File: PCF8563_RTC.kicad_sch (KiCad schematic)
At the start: 28 parts, among them J1 CONN_2P, J2 CONN_2P, J3 CONN_2P, J4 CONN_2P, J5 CONN_2P, J6 CONN_2P, J7 CONN_2P, U1 PCF8563, X1 32.768 kHz

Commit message: Created footprints for the PCF8563-SO8 package and capacitors
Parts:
- C1, C2, C3, C4: footprint (none) -> workshop_footprints:C0603
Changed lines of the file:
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@@
       (effects (font (size 1.27 1.27)) (justify right))
     )
-    (property "Footprint" "" (id 2) (at 61.595 50.8 0)
+    (property "Footprint" "workshop_footprints:C0603" (id 2) (at 61.595 50.8 0)
       (effects (font (size 1.27 1.27)) hide)
     )
@@
       (effects (font (size 1.27 1.27)) (justify right))
     )
-    (property "Footprint" "" (id 2) (at 32.385 116.84 0)
+    (property "Footprint" "workshop_footprints:C0603" (id 2) (at 32.385 116.84 0)
       (effects (font (size 1.27 1.27)) hide)
     )
@@
     (pin "2")
   )
-  (symbol (lib_id "WorkshopSymbols:C") (at 98.425 88.9 90) (unit 1)
+  (symbol (lib_name "C_3") (lib_id "WorkshopSymbols:C") (at 98.425 88.9 90) (unit 1)
     (in_bom yes) (on_board yes)
     (property "Reference" "C4" (id 0) (at 100.965 87.6299 90)
@@
       (effects (font (size 1.27 1.27)) (justify right))
     )
-    (property "Footprint" "" (id 2) (at 94.615 93.98 0)
+    (property "Footprint" "workshop_footprints:C0603" (id 2) (at 94.615 93.98 0)
       (effects (font (size 1.27 1.27)) hide)
     )
@@
       (effects (font (size 1.27 1.27)) (justify right))
     )
-    (property "Footprint" "" (id 2) (at 45.085 116.84 0)
+    (property "Footprint" "workshop_footprints:C0603" (id 2) (at 45.085 116.84 0)
       (effects (font (size 1.27 1.27)) hide)
     )
@@
     )
     (path "/8982208d-042b-48e9-a73e-04fa77665b85"
-      (reference "C1") (unit 1) (value "10pF 1%") (footprint "")
+      (reference "C1") (unit 1) (value "10pF 1%") (footprint "workshop_footprints:C0603")
     )
     (path "/98f85ca1-8d67-4856-903d-689ae5bc7163"
-      (reference "C2") (unit 1) (value "10pF 1%") (footprint "")
+      (reference "C2") (unit 1) (value "10pF 1%") (footprint "workshop_footprints:C0603")
     )
     (path "/41296beb-b987-4190-941b-e29783d80155"
-      (reference "C3") (unit 1) (value "100nF") (footprint "")
+      (reference "C3") (unit 1) (value "100nF") (footprint "workshop_footprints:C0603")
     )
     (path "/95eea291-064d-424f-aac4-a84523beff96"
-      (reference "C4") (unit 1) (value "100nF") (footprint "")
+      (reference "C4") (unit 1) (value "100nF") (footprint "workshop_footprints:C0603")
     )
     (path "/ff1a9192-9a7b-4f71-b206-b5573f62f98c"

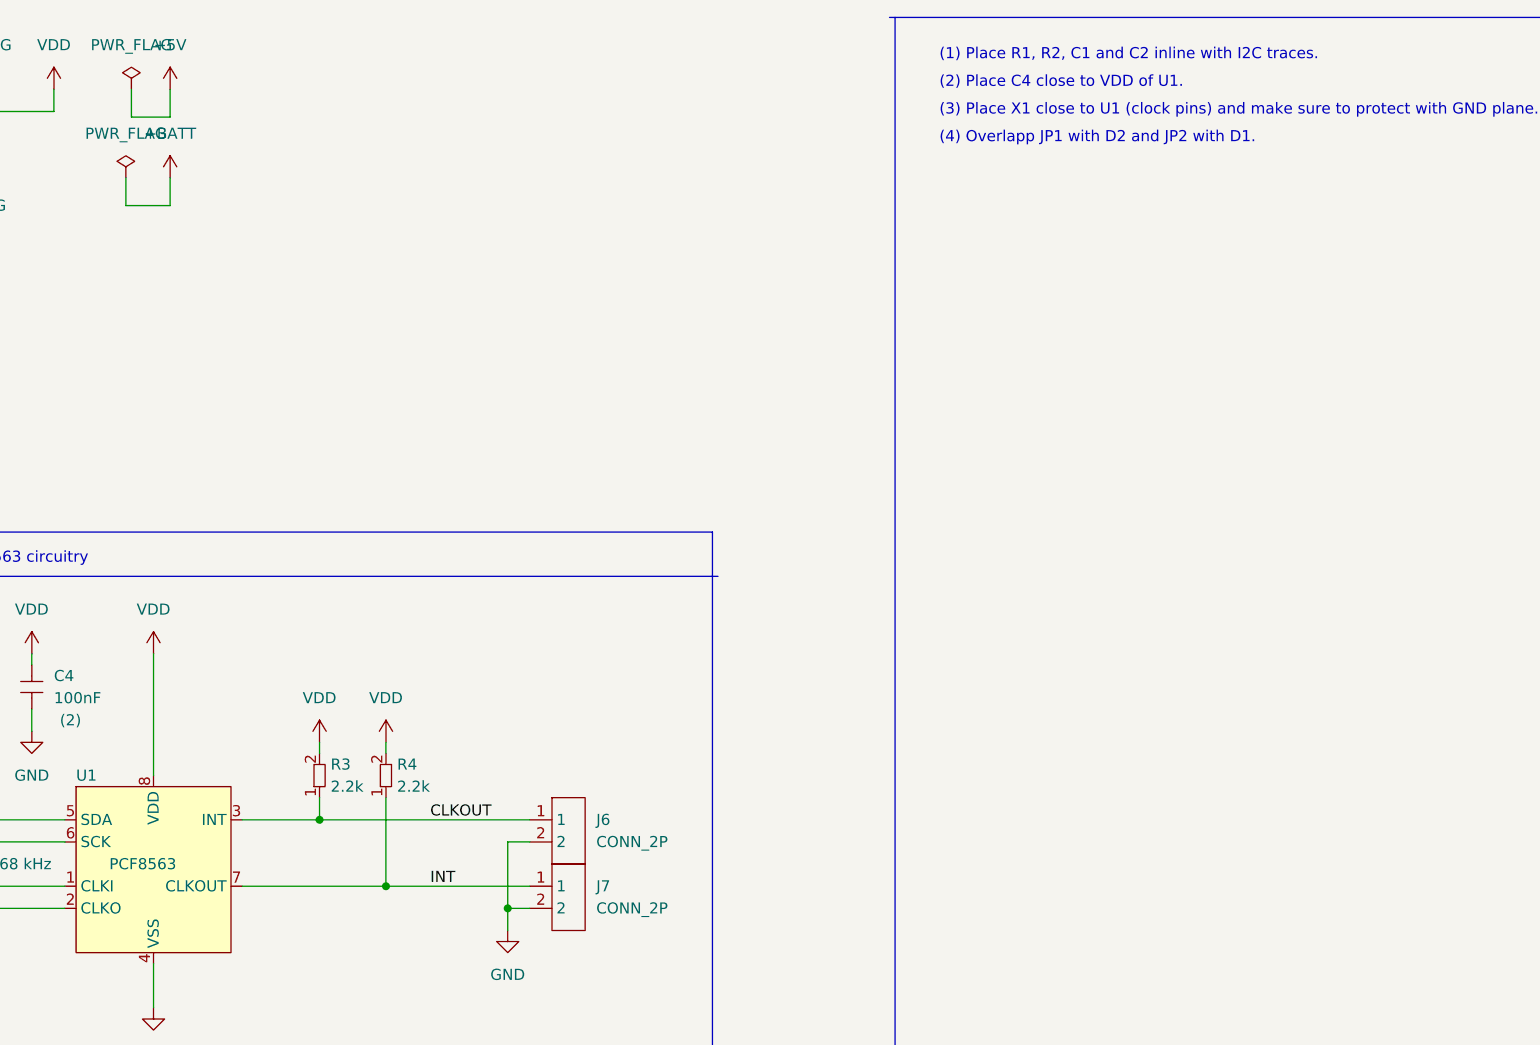
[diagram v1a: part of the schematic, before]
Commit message: Finished PCB layout and routing
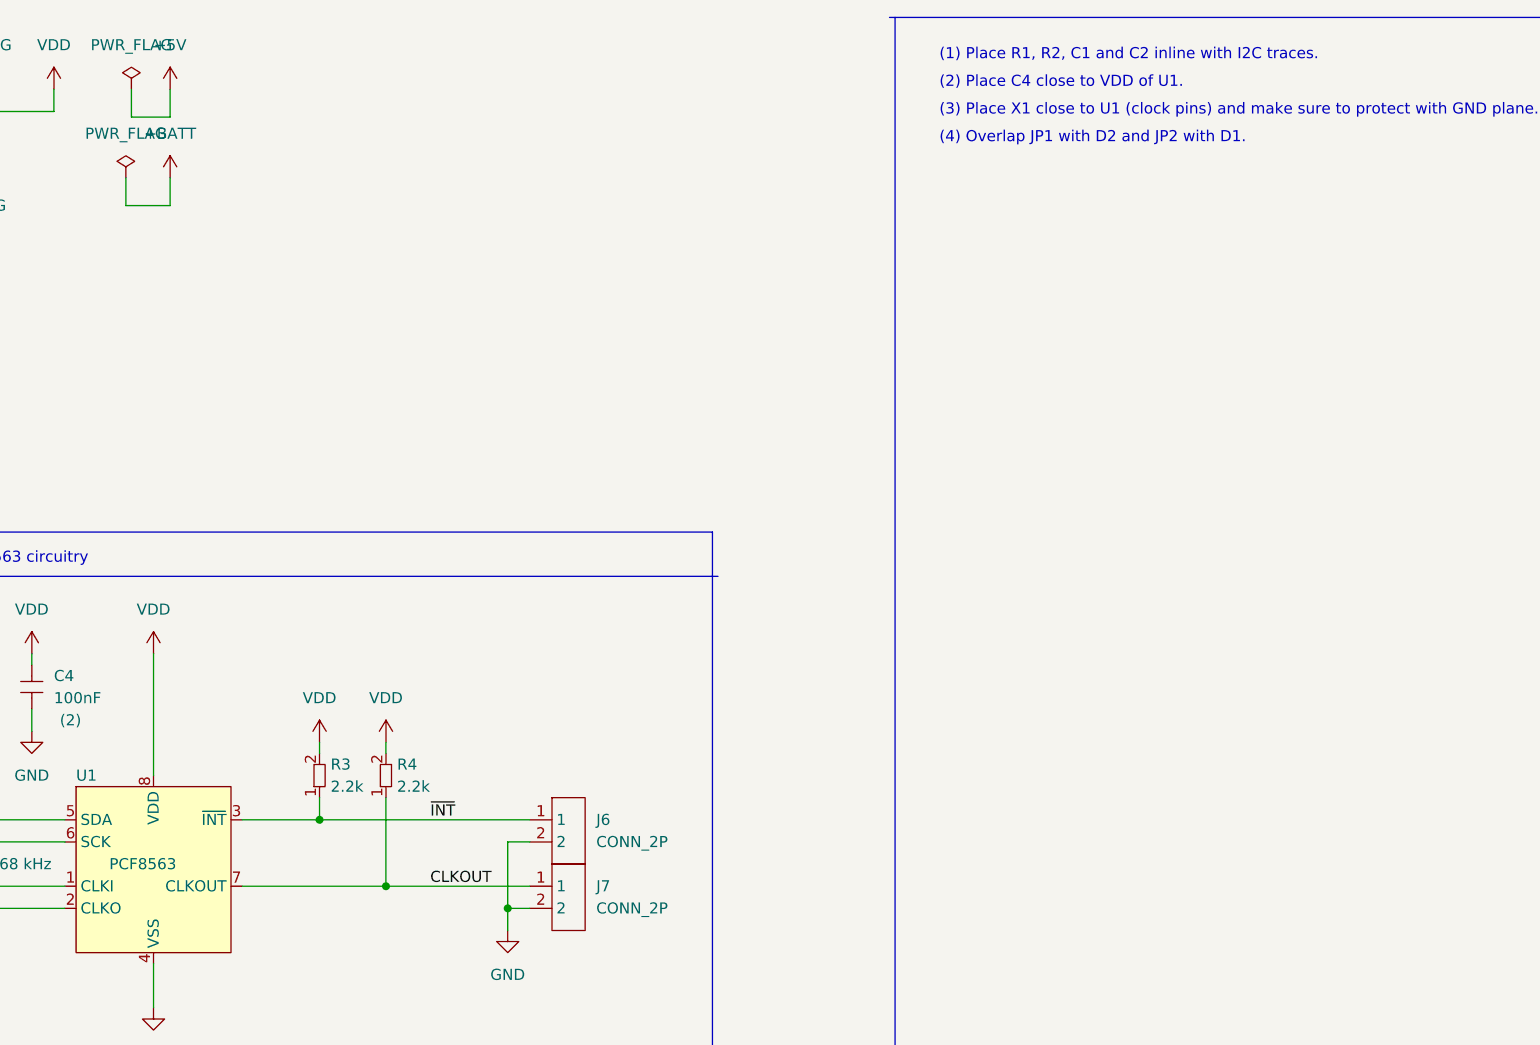
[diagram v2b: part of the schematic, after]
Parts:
- FID1, FID2, FID3: footprint (none) -> Fiducial:Fiducial_0.5mm_Mask1.5mm
- H1, H2, H3, H4: footprint (none) -> footprints:MountingHole_3.2mm_M3
- J1, J2, J3, J4, J5, J6, J7: footprint (none) -> workshop_footprints:CONN_2P
- JP1, JP2: footprint (none) -> Jumper:SolderJumper-2_P1.3mm_Bridged2Bar_Pad1.0x1.5mm
- U1: footprint (none) -> workshop_footprints:PCF8563_SO8
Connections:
- net INT is gone; now on net CLKOUT: J7.1, R4.1, U1.7 (CLKOUT)
- net CLKOUT: no longer J6.1, R3.1, U1.3 (INT)
- new net ~{INT}: J6.1, R3.1, U1.3 (~{INT})
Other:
- note added: "(4) Overlap JP1 with D2 and JP2 with D1."
- note removed: "(4) Overlapp JP1 with D2 and JP2 with D1."
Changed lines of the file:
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@@
     (effects (font (size 1.27 1.27)) (justify left bottom))
   )
-  (text "(4) Overlapp JP1 with D2 and JP2 with D1." (at 202.565 26.67 0)
+  (text "(4) Overlap JP1 with D2 and JP2 with D1." (at 202.565 26.67 0)
     (effects (font (size 1.27 1.27)) (justify left bottom))
   )
-  (label "INT" (at 144.145 111.76 0)
+  (label "CLKOUT" (at 144.145 111.76 0)
     (effects (font (size 1.27 1.27)) (justify left bottom))
   )
@@
     (effects (font (size 1.27 1.27)) (justify left bottom))
   )
-  (label "CLKOUT" (at 144.145 104.14 0)
+  (label "~{INT}" (at 144.145 104.14 0)
     (effects (font (size 1.27 1.27)) (justify left bottom))
   )
@@
       (effects (font (size 1.27 1.27)) (justify left))
     )
-    (property "Footprint" "" (id 2) (at 27.305 176.53 0)
+    (property "Footprint" "footprints:MountingHole_3.2mm_M3" (id 2) (at 27.305 176.53 0)
       (effects (font (size 1.27 1.27)) hide)
     )
@@
       (effects (font (size 1.27 1.27)) hide)
     )
-    (property "Footprint" "" (id 2) (at 47.625 40.64 0)
+    (property "Footprint" "Jumper:SolderJumper-2_P1.3mm_Bridged2Bar_Pad1.0x1.5mm" (id 2) (at 47.625 40.64 0)
       (effects (font (size 1.27 1.27)) hide)
     )
@@
       (effects (font (size 1.27 1.27)) (justify left))
     )
-    (property "Footprint" "" (id 2) (at 57.15 187.96 0)
+    (property "Footprint" "footprints:MountingHole_3.2mm_M3" (id 2) (at 57.15 187.96 0)
       (effects (font (size 1.27 1.27)) hide)
     )
@@
     (property "Reference" "J2" (id 0) (at 25.4 80.01 0))
     (property "Value" "CONN_2P" (id 1) (at 25.4 82.55 0))
-    (property "Footprint" "" (id 2) (at 29.845 87.63 0)
+    (property "Footprint" "workshop_footprints:CONN_2P" (id 2) (at 29.845 87.63 0)
       (effects (font (size 1.27 1.27)) hide)
     )
@@
       (effects (font (size 1.27 1.27)) (justify left))
     )
-    (property "Footprint" "" (id 2) (at 102.235 104.14 0)
+    (property "Footprint" "workshop_footprints:PCF8563_SO8" (id 2) (at 102.235 104.14 0)
       (effects (font (size 1.27 1.27)) hide)
     )
@@
     (property "Reference" "J4" (id 0) (at 26.67 29.21 0))
     (property "Value" "CONN_2P" (id 1) (at 26.67 31.75 0))
-    (property "Footprint" "" (id 2) (at 31.115 36.83 0)
+    (property "Footprint" "workshop_footprints:CONN_2P" (id 2) (at 31.115 36.83 0)
       (effects (font (size 1.27 1.27)) hide)
     )
@@
       (effects (font (size 1.27 1.27)) hide)
     )
-    (property "Footprint" "" (id 2) (at 46.355 57.785 0)
+    (property "Footprint" "Jumper:SolderJumper-2_P1.3mm_Bridged2Bar_Pad1.0x1.5mm" (id 2) (at 46.355 57.785 0)
       (effects (font (size 1.27 1.27)) hide)
     )
@@
       (effects (font (size 1.27 1.27)) (justify left))
     )
-    (property "Footprint" "" (id 2) (at 83.82 162.56 0)
+    (property "Footprint" "Fiducial:Fiducial_0.5mm_Mask1.5mm" (id 2) (at 83.82 162.56 0)
       (effects (font (size 1.27 1.27)) hide)
     )
@@
       (effects (font (size 1.27 1.27)) (justify left))
     )
-    (property "Footprint" "" (id 2) (at 86.995 176.53 0)
+    (property "Footprint" "Fiducial:Fiducial_0.5mm_Mask1.5mm" (id 2) (at 86.995 176.53 0)
       (effects (font (size 1.27 1.27)) hide)
     )
@@
       (effects (font (size 1.27 1.27)) (justify left))
     )
-    (property "Footprint" "" (id 2) (at 155.575 104.14 0)
+    (property "Footprint" "workshop_footprints:CONN_2P" (id 2) (at 155.575 104.14 0)
       (effects (font (size 1.27 1.27)) hide)
     )
@@
     (property "Reference" "J5" (id 0) (at 26.67 43.18 0))
     (property "Value" "CONN_2P" (id 1) (at 26.67 45.72 0))
-    (property "Footprint" "" (id 2) (at 31.115 50.8 0)
+    (property "Footprint" "workshop_footprints:CONN_2P" (id 2) (at 31.115 50.8 0)
       (effects (font (size 1.27 1.27)) hide)
     )
@@
       (effects (font (size 1.27 1.27)) (justify left))
     )
-    (property "Footprint" "" (id 2) (at 57.15 175.895 0)
+    (property "Footprint" "footprints:MountingHole_3.2mm_M3" (id 2) (at 57.15 175.895 0)
       (effects (font (size 1.27 1.27)) hide)
     )
@@
     (property "Reference" "J1" (id 0) (at 24.13 133.35 0))
     (property "Value" "CONN_2P" (id 1) (at 24.13 135.89 0))
-    (property "Footprint" "" (id 2) (at 28.575 140.97 0)
+    (property "Footprint" "workshop_footprints:CONN_2P" (id 2) (at 28.575 140.97 0)
       (effects (font (size 1.27 1.27)) hide)
     )
@@
       (effects (font (size 1.27 1.27)) (justify left))
     )
-    (property "Footprint" "" (id 2) (at 155.575 111.76 0)
+    (property "Footprint" "workshop_footprints:CONN_2P" (id 2) (at 155.575 111.76 0)
       (effects (font (size 1.27 1.27)) hide)
     )
@@
     (property "Reference" "J3" (id 0) (at 25.4 96.52 0))
     (property "Value" "CONN_2P" (id 1) (at 25.4 99.06 0))
-    (property "Footprint" "" (id 2) (at 29.845 104.14 0)
+    (property "Footprint" "workshop_footprints:CONN_2P" (id 2) (at 29.845 104.14 0)
       (effects (font (size 1.27 1.27)) hide)
     )
@@
       (effects (font (size 1.27 1.27)) (justify left))
     )
-    (property "Footprint" "" (id 2) (at 92.71 168.91 0)
+    (property "Footprint" "Fiducial:Fiducial_0.5mm_Mask1.5mm" (id 2) (at 92.71 168.91 0)
       (effects (font (size 1.27 1.27)) hide)
     )
@@
       (effects (font (size 1.27 1.27)) (justify left))
     )
-    (property "Footprint" "" (id 2) (at 26.67 188.595 0)
+    (property "Footprint" "footprints:MountingHole_3.2mm_M3" (id 2) (at 26.67 188.595 0)
       (effects (font (size 1.27 1.27)) hide)
     )
@@
     )
     (path "/801bf3b6-8d0d-48d0-9a60-3d1a76f41508"
-      (reference "FID1") (unit 1) (value "Fiducial") (footprint "")
+      (reference "FID1") (unit 1) (value "Fiducial") (footprint "Fiducial:Fiducial_0.5mm_Mask1.5mm")
     )
     (path "/f88856ee-4a1a-4ba9-bdbb-491fd14736cb"
-      (reference "FID2") (unit 1) (value "Fiducial") (footprint "")
+      (reference "FID2") (unit 1) (value "Fiducial") (footprint "Fiducial:Fiducial_0.5mm_Mask1.5mm")
     )
     (path "/8b45d3f8-3983-43b6-8a28-686cdd80f2b8"
-      (reference "FID3") (unit 1) (value "Fiducial") (footprint "")
+      (reference "FID3") (unit 1) (value "Fiducial") (footprint "Fiducial:Fiducial_0.5mm_Mask1.5mm")
     )
     (path "/07586f57-2849-4baa-92f1-2a6ff9d8d68e"
-      (reference "H1") (unit 1) (value "MountingHole_Pad") (footprint "")
+      (reference "H1") (unit 1) (value "MountingHole_Pad") (footprint "footprints:MountingHole_3.2mm_M3")
     )
     (path "/d8bf0370-4ba0-4304-b752-8665cf26c9de"
-      (reference "H2") (unit 1) (value "MountingHole_Pad") (footprint "")
+      (reference "H2") (unit 1) (value "MountingHole_Pad") (footprint "footprints:MountingHole_3.2mm_M3")
     )
     (path "/f8da16ca-b534-499d-a232-78a8461a683a"
-      (reference "H3") (unit 1) (value "MountingHole_Pad") (footprint "")
+      (reference "H3") (unit 1) (value "MountingHole_Pad") (footprint "footprints:MountingHole_3.2mm_M3")
     )
     (path "/20957906-790b-4b25-964c-1a00d3c78bb3"
-      (reference "H4") (unit 1) (value "MountingHole_Pad") (footprint "")
+      (reference "H4") (unit 1) (value "MountingHole_Pad") (footprint "footprints:MountingHole_3.2mm_M3")
     )
     (path "/da3f2b28-9e2a-4b73-8afc-344bb9b072fe"
-      (reference "J1") (unit 1) (value "CONN_2P") (footprint "")
+      (reference "J1") (unit 1) (value "CONN_2P") (footprint "workshop_footprints:CONN_2P")
     )
     (path "/4031b380-22e2-42d0-8c81-ca49041117a8"
-      (reference "J2") (unit 1) (value "CONN_2P") (footprint "")
+      (reference "J2") (unit 1) (value "CONN_2P") (footprint "workshop_footprints:CONN_2P")
     )
     (path "/ea98fa7a-d62f-4e2b-bf3e-1671b81640af"
-      (reference "J3") (unit 1) (value "CONN_2P") (footprint "")
+      (reference "J3") (unit 1) (value "CONN_2P") (footprint "workshop_footprints:CONN_2P")
     )
     (path "/49df19aa-61ce-4a79-9946-533deb99e69e"
-      (reference "J4") (unit 1) (value "CONN_2P") (footprint "")
+      (reference "J4") (unit 1) (value "CONN_2P") (footprint "workshop_footprints:CONN_2P")
     )
     (path "/95c784d5-650d-4b18-bbf4-9a3bf8077c2d"
-      (reference "J5") (unit 1) (value "CONN_2P") (footprint "")
+      (reference "J5") (unit 1) (value "CONN_2P") (footprint "workshop_footprints:CONN_2P")
     )
     (path "/956a3513-c050-46ca-bc33-d76ffe8163f4"
-      (reference "J6") (unit 1) (value "CONN_2P") (footprint "")
+      (reference "J6") (unit 1) (value "CONN_2P") (footprint "workshop_footprints:CONN_2P")
     )
     (path "/ddc71168-6b08-4ca4-804d-4c7d7d4e17e7"
-      (reference "J7") (unit 1) (value "CONN_2P") (footprint "")
+      (reference "J7") (unit 1) (value "CONN_2P") (footprint "workshop_footprints:CONN_2P")
     )
     (path "/4ce951e9-3269-49cf-8a0a-b070a62a3c40"
-      (reference "JP1") (unit 1) (value "SolderJumper_2_Open") (footprint "")
+      (reference "JP1") (unit 1) (value "SolderJumper_2_Open") (footprint "Jumper:SolderJumper-2_P1.3mm_Bridged2Bar_Pad1.0x1.5mm")
     )
     (path "/17529757-2160-42e0-bec7-015e2b15cc93"
-      (reference "JP2") (unit 1) (value "SolderJumper_2_Open") (footprint "")
+      (reference "JP2") (unit 1) (value "SolderJumper_2_Open") (footprint "Jumper:SolderJumper-2_P1.3mm_Bridged2Bar_Pad1.0x1.5mm")
     )
     (path "/2d62e045-1966-49c4-bb1c-a93b1eab7e43"
@@
     )
     (path "/434febe2-55c1-4ef1-b181-d9a4803f5601"
-      (reference "U1") (unit 1) (value "PCF8563") (footprint "")
+      (reference "U1") (unit 1) (value "PCF8563") (footprint "workshop_footprints:PCF8563_SO8")
     )
     (path "/8541e3c5-f2d4-49ae-9eae-f4a7e259cb64"
